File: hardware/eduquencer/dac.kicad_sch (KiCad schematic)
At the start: 14 parts

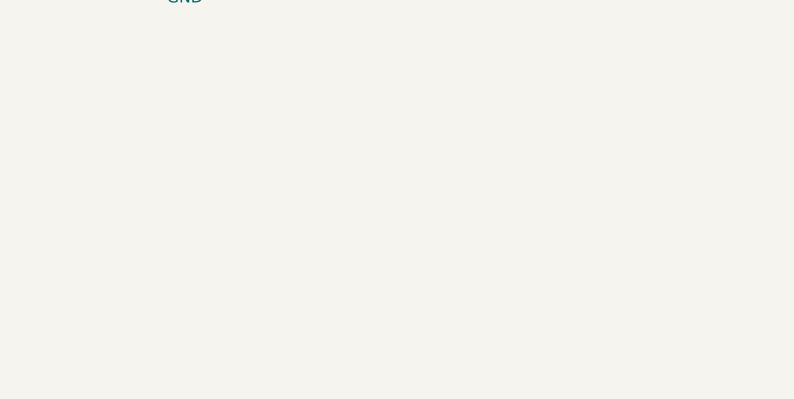
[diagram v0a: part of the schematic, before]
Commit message: add DAC80501MDGST model
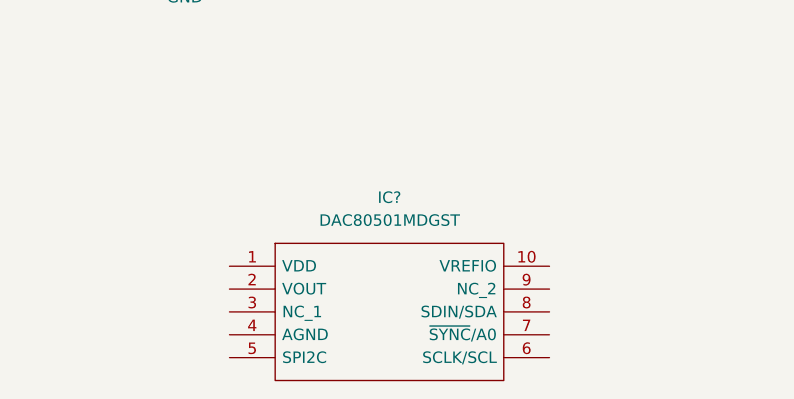
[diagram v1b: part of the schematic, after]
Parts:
- added IC?: DAC80501MDGST, SOP50P490X110-10N, symbol DAC80501MDGST:DAC80501MDGST
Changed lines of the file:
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@@
     (pin "1")
   )
+  (symbol (lib_id "DAC80501MDGST:DAC80501MDGST") (at 57.15 142.24 0) (unit 1)
+    (in_bom yes) (on_board yes) (fields_autoplaced)
+    (property "Reference" "IC?" (id 0) (at 74.93 134.62 0))
+    (property "Value" "DAC80501MDGST" (id 1) (at 74.93 137.16 0))
+    (property "Footprint" "SOP50P490X110-10N" (id 2) (at 88.9 139.7 0)
+      (effects (font (size 1.27 1.27)) (justify left) hide)
+    )
+    (property "Datasheet" "https://www.ti.com/lit/gpn/DAC80501" (id 3) (at 88.9 142.24 0)
+      (effects (font (size 1.27 1.27)) (justify left) hide)
+    )
+    (property "Description" "Digital to Analog Converters - DAC True 16-bit, 1-ch, SPI/I2C, voltage-output DAC in WSON package with precision internal reference 10-VSSOP -40 to 125" (id 4) (at 88.9 144.78 0)
+      (effects (font (size 1.27 1.27)) (justify left) hide)
+    )
+    (property "Height" "1.1" (id 5) (at 88.9 147.32 0)
+      (effects (font (size 1.27 1.27)) (justify left) hide)
+    )
+    (property "Manufacturer_Name" "Texas Instruments" (id 6) (at 88.9 149.86 0)
+      (effects (font (size 1.27 1.27)) (justify left) hide)
+    )
+    (property "Manufacturer_Part_Number" "DAC80501MDGST" (id 7) (at 88.9 152.4 0)
+      (effects (font (size 1.27 1.27)) (justify left) hide)
+    )
+    (property "Mouser Part Number" "595-DAC80501MDGST" (id 8) (at 88.9 154.94 0)
+      (effects (font (size 1.27 1.27)) (justify left) hide)
+    )
+    (property "Mouser Price/Stock" "https://www.mouser.co.uk/ProductDetail/Texas-Instruments/DAC80501MDGST?qs=%252B6g0mu59x7I7TnYkBjkntw%3D%3D" (id 9) (at 88.9 157.48 0)
+      (effects (font (size 1.27 1.27)) (justify left) hide)
+    )
+    (property "Arrow Part Number" "DAC80501MDGST" (id 10) (at 88.9 160.02 0)
+      (effects (font (size 1.27 1.27)) (justify left) hide)
+    )
+    (property "Arrow Price/Stock" "https://www.arrow.com/en/products/dac80501mdgst/texas-instruments?region=nac" (id 11) (at 88.9 162.56 0)
+      (effects (font (size 1.27 1.27)) (justify left) hide)
+    )
+    (pin "1")
+    (pin "10")
+    (pin "2")
+    (pin "3")
+    (pin "4")
+    (pin "5")
+    (pin "6")
+    (pin "7")
+    (pin "8")
+    (pin "9")
+  )
 )

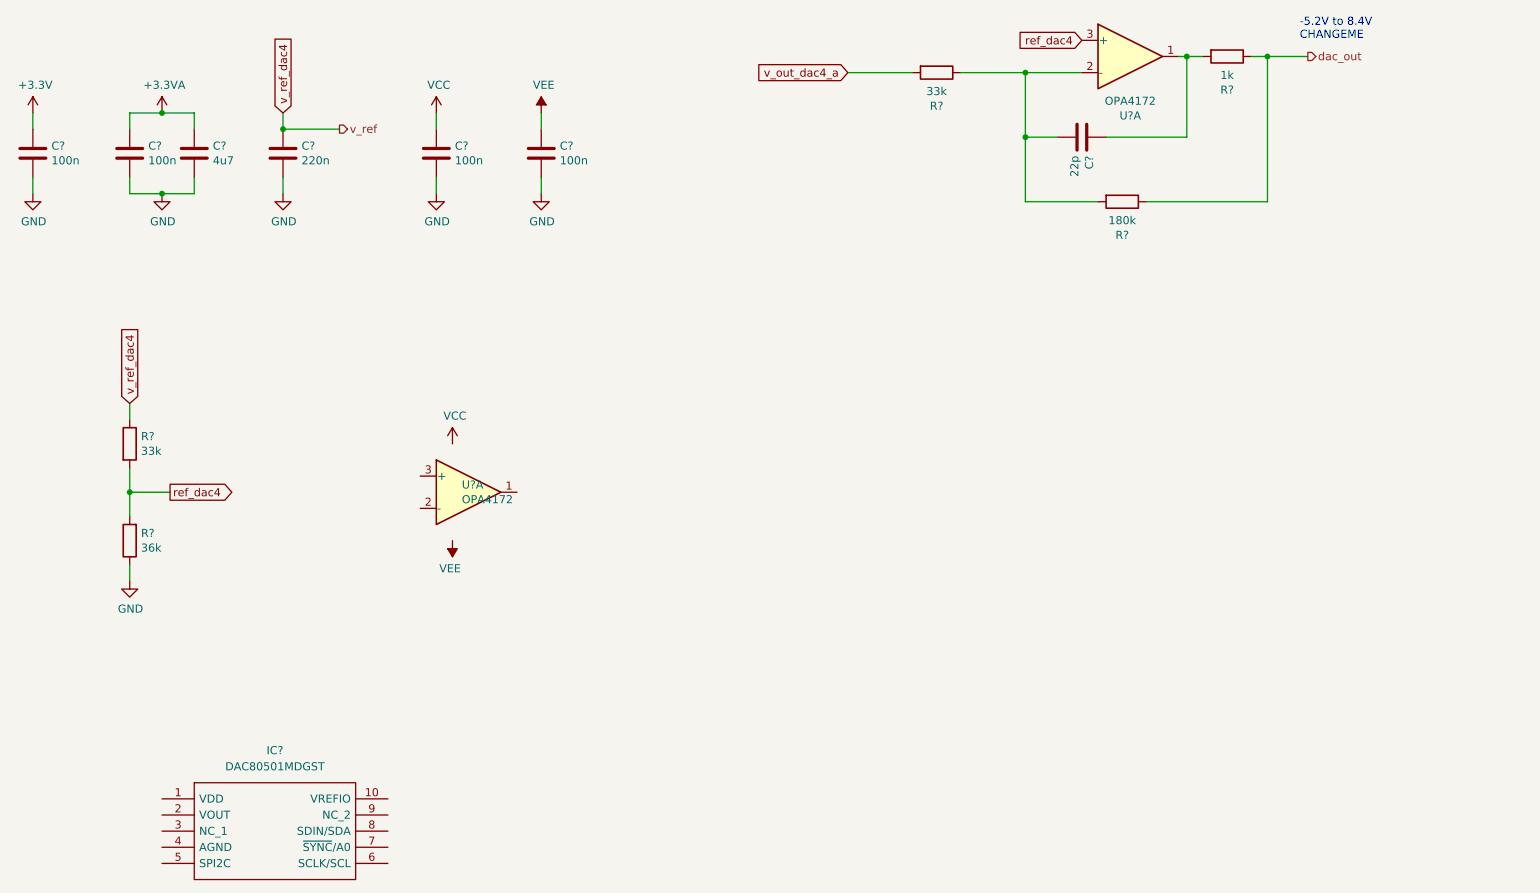
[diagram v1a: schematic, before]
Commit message: add DAC schematic
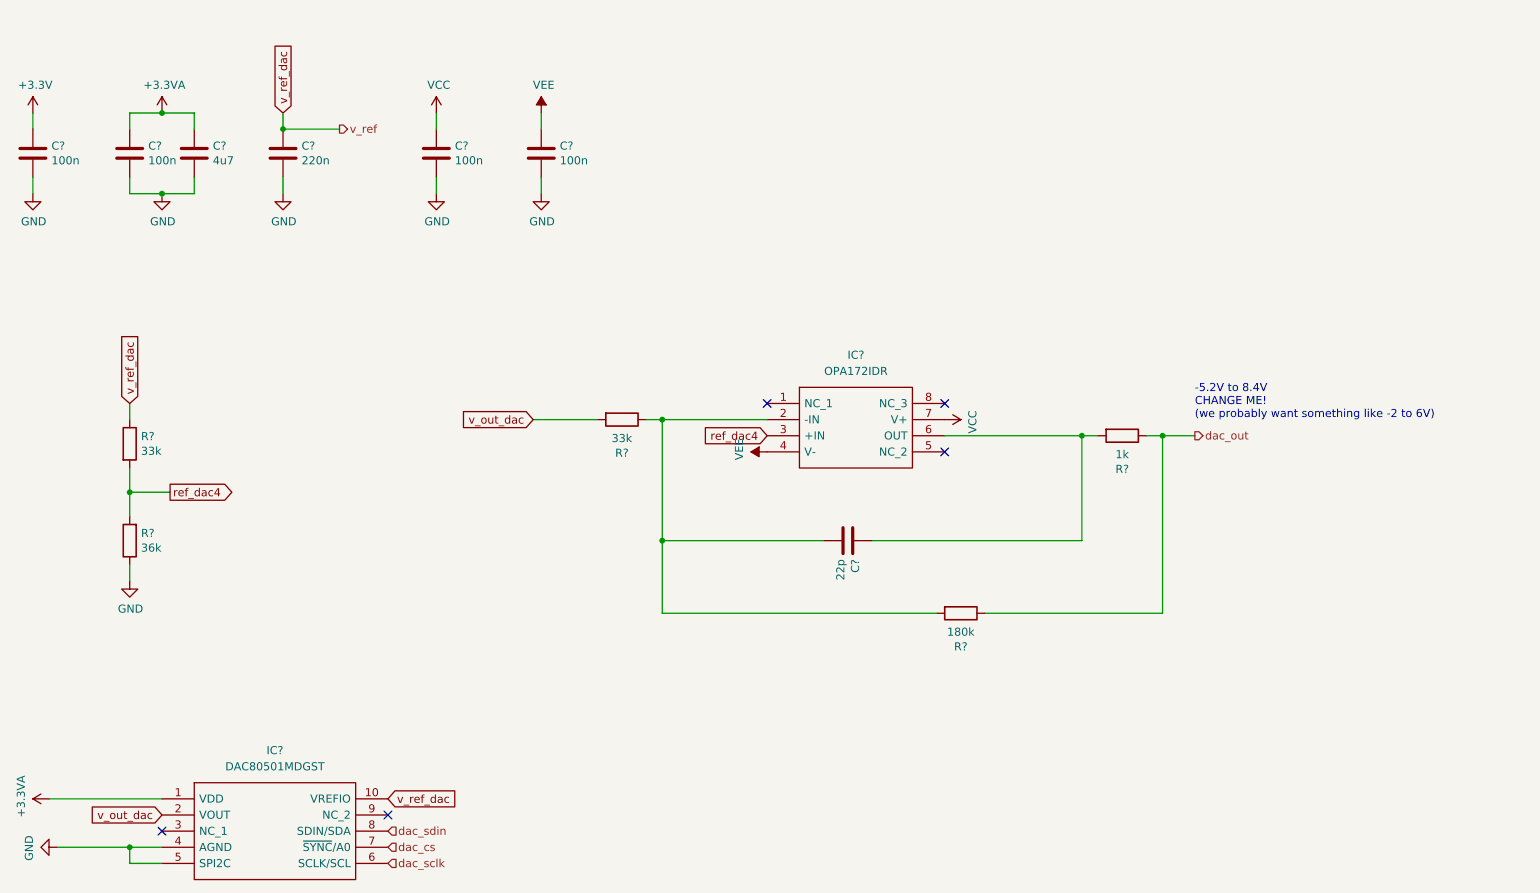
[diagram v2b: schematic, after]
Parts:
- removed U? (x2): OPA4172, Package_SO:TSSOP-14_4.4x5mm_P0.65mm, symbol Amplifier_Operational:TL074
- added IC?: OPA172IDR, SOIC127P600X175-8N, symbol OPA172IDR:OPA172IDR
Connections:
- net v_out_dac4_a is gone; now on net v_out_dac: R?.2
- net v_ref_dac4 is gone; now on net v_ref_dac: C?.2, R?.1
- net +3.3VA: now also IC?.1 (VDD)
- net GND: now also IC?.4 (AGND), IC?.5 (SPI2C)
- net VCC: now also IC?.7 (V+)
- net VEE: now also IC?.4 (V-)
- net ref_dac4: now also IC?.3 (+IN)
- net at C?.1, R?.1, R?.2: now also IC?.2 (-IN)
- net at C?.2, R?.2: now also IC?.6 (OUT)
- net v_ref_dac: now reaches IC?.10 (VREFIO)
- net v_out_dac: now reaches IC?.2 (VOUT)
- net dac_sclk: now reaches IC?.6 (SCLK/SCL)
- net dac_cs: now reaches IC?.7 (~{SYNC}/A0)
- net dac_sdin: now reaches IC?.8 (SDIN/SDA)
- no-connect marks 0 -> 5
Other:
- note added: "-5.2V to 8.4V CHANGE ME! (we probably want something like -2 to 6V)"
- note removed: "-5.2V to 8.4V CHANGEME"
- moved on the sheet: C?, R?
